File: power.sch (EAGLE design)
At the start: 7 parts, among them U1 LT3652

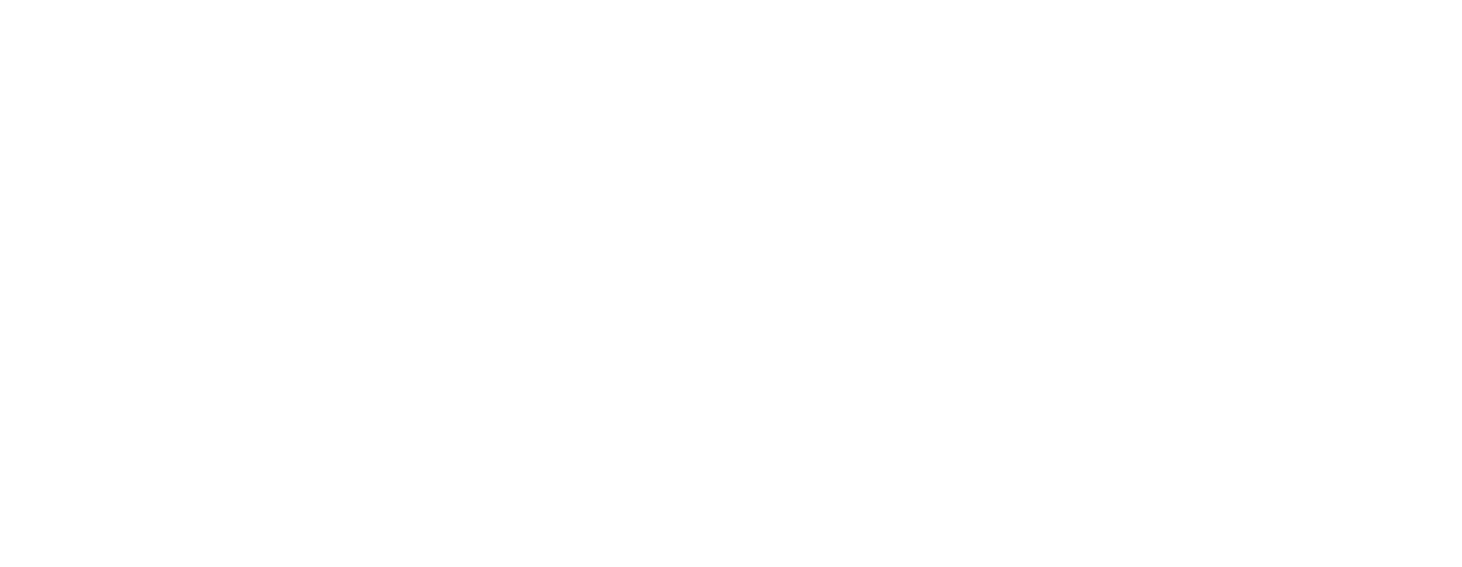
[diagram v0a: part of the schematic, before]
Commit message: Added RTC backup batteries
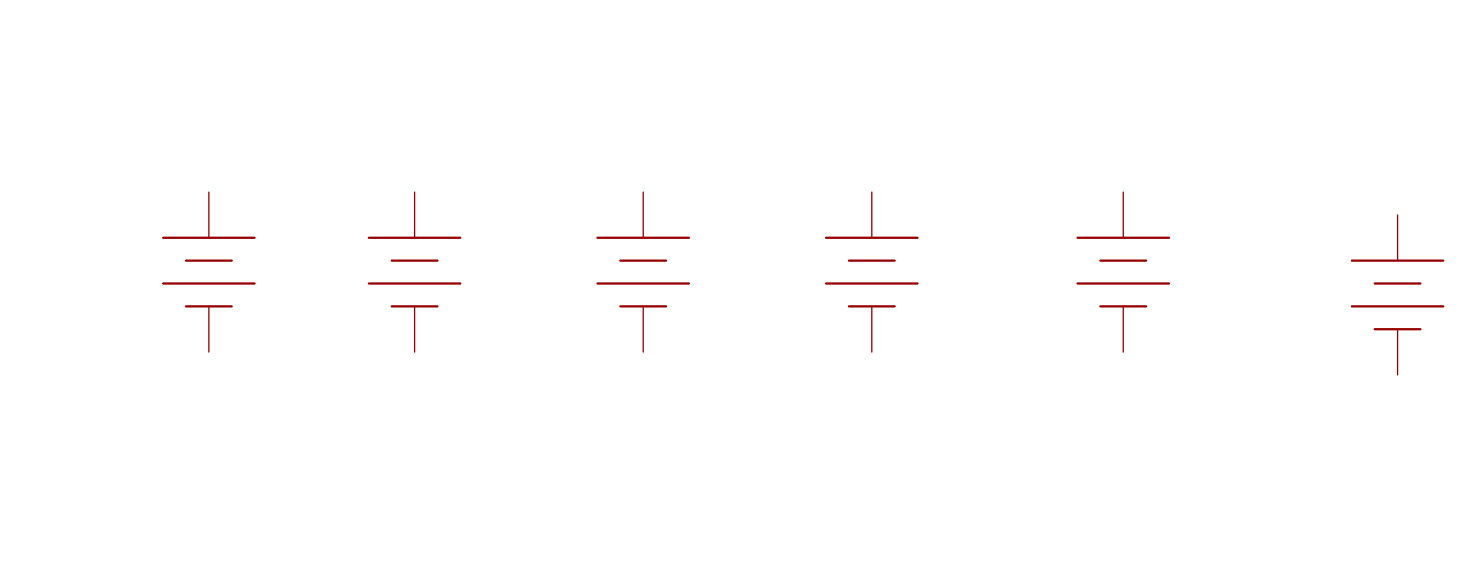
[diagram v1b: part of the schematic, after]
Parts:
- added U$10, U$11, U$12, U$7, U$8, U$9: BETABATTERY, Widetronix:BETABATTERY
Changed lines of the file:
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@@
 <part name="U$5" library="G125-FV20605L0P" deviceset="G125-FV20605L0P" device=""/>
 <part name="U$6" library="G125-FV20605L0P" deviceset="G125-FV20605L0P" device=""/>
+<part name="U$7" library="Widetronix" deviceset="BETABATTERY" device=""/>
+<part name="U$8" library="Widetronix" deviceset="BETABATTERY" device=""/>
+<part name="U$9" library="Widetronix" deviceset="BETABATTERY" device=""/>
+<part name="U$10" library="Widetronix" deviceset="BETABATTERY" device=""/>
+<part name="U$11" library="Widetronix" deviceset="BETABATTERY" device=""/>
+<part name="U$12" library="Widetronix" deviceset="BETABATTERY" device=""/>
 </parts>
 <sheets>
@@
 <instance part="U$5" gate="G$1" x="73.66" y="81.28" rot="R90"/>
 <instance part="U$6" gate="G$1" x="114.3" y="86.36" rot="R90"/>
+<instance part="U$7" gate="G$1" x="167.64" y="66.04"/>
+<instance part="U$8" gate="G$1" x="190.5" y="66.04"/>
+<instance part="U$9" gate="G$1" x="215.9" y="66.04"/>
+<instance part="U$10" gate="G$1" x="241.3" y="66.04"/>
+<instance part="U$11" gate="G$1" x="269.24" y="66.04"/>
+<instance part="U$12" gate="G$1" x="299.72" y="63.5"/>
 </instances>
 <busses>

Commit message: Power board work
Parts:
- added H1, H2: PINHD-2X26, SparkFun-Connectors:PINHD-2X26
- added J1: POWER_JACKPTH_BREAD, SparkFun-Connectors:POWER_JACKPTH_BREAD
- added JP1, JP2, JP3: M025MM, SparkFun-Connectors:M025MM
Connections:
- new net 3.3V: H2.27, H2.28
- new net 5V: H2.25, H2.26
- new net GND: H2.29, H2.30, H2.31, H2.32, J1.GND, J1.GNDBREAK, JP1.1, JP2.1, JP3.1, U$10.V-, U$11.V-, U$12.V-, U$7.V-, U$8.V-, U$9.V-, U1.GND_PAD
- new net SCL: H1.43
- new net SDA: H1.41
- new net VBACKUP: H1.42, U$10.V+, U$11.V+, U$12.V+, U$7.V+, U$8.V+, U$9.V+
- new net VBATT: H2.45, H2.46, J1.PWR, JP1.2, JP2.2
- new net VBURN3: JP3.2

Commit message: Added LT3688 dual regulator
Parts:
- added C1, C2, C30: .1uF, phonesat:CAPACITOR0805
- added R1, R25, R31, R4, R5, R8: 0R, phonesat:RESISTOR2512
- added R2, R27, R6: 3K3, phonesat:RESISTOR0805
- added R28, R3, R7: 10K, phonesat:RESISTOR0805
- added T1, T2, T3: SINGLE_NCHAN_FET, phonesat:SINGLE_NCHAN_FET
- added U$13: LT3688, LT3688:LT3688
- added U14, U2: MOSFET_PCHAN_20A, phonesat:MOSFET_PCHAN_20A
- U1: value LT3652 -> MOSFET_PCHAN_20A; device SparkFun-PowerIC:LT3652 -> phonesat:MOSFET_PCHAN_20A
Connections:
- new net ENAB_BURN1: R28.1, R3.1, R7.1
- new net N$1: R1.2, R4.2, U1.S@1, U1.S@2, U1.S@3
- new net N$19: R25.2, R31.2, U14.S@1, U14.S@2, U14.S@3
- new net N$2: C1.1, R3.2, T1.G
- new net N$21: C30.1, R28.2, T2.G
- new net N$24: R27.1, T2.D, U14.G
- new net N$3: R2.1, T1.D, U1.G
- new net N$4: R5.2, R8.2, U2.S@1, U2.S@2, U2.S@3
- new net N$5: C2.1, R7.2, T3.G
- new net N$6: R6.1, T3.D, U2.G
- new net VBURN1: U14.D@1, U14.D@2, U14.D@3, U14.D@4
- new net VBURN2: U1.D@1, U1.D@2, U1.D@3, U1.D@4
- new net VCC_8: R1.1, R2.2, R25.1, R27.2, R31.1, R4.1, R5.1, R6.2, R8.1
- new net VSOLAR: U$5.P3, U$5.P6
- net GND: now also C1.2, C2.2, C30.2, T1.S, T2.S, T3.S, U$1.P1, U$1.P4, U$2.P1, U$2.P4, U$3.P1, U$3.P4, U$4.P1, U$4.P4, U$5.P1, U$5.P4, U$6.P1, U$6.P4; no longer U1.GND_PAD
- net VBURN3: now also U2.D@1, U2.D@2, U2.D@3, U2.D@4
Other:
- note added: "BW1"
- note added: "BW2"
- note added: "BW3"

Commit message: More switching regulator work
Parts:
- added C3, C4, C5: 0.22uF, SparkFun-Capacitors:CAP0805
- added C31, C32: .1uF, phonesat:CAPACITOR0805
- added C6, C7: 10pF, SparkFun-Capacitors:CAP0805
- added C8, C9: 1nF, SparkFun-Capacitors:CAP0805
- added R11: 523k, SparkFun-Resistors:RESISTOR0805-RES
- added R12, R14: 100k, SparkFun-Resistors:RESISTOR0805-RES
- added R13: 316k, SparkFun-Resistors:RESISTOR0805-RES
- added R9: 10k, SparkFun-Resistors:RESISTOR0805-RES
- C1: value .1uF -> 4.7uF; device phonesat:CAPACITOR0805 -> SparkFun-Capacitors:CAP0805
- C2: value .1uF -> 0.22uF; device phonesat:CAPACITOR0805 -> SparkFun-Capacitors:CAP0805
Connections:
- new net N$11: C3.1, U$13.BST2
- new net N$12: C6.2, R11.1, R12.2, U$13.FB1
- new net N$13: C8.2, U$13.RUNSS1
- new net N$14: C7.2, R13.1, R14.2, U$13.FB2
- new net N$7: R9.1, U$13.EN
- new net N$8: C9.1, U$13.RUNSS2
- new net N$9: C2.1, U$13.BST1
- net 3.3V: now also C3.2, C5.1, C7.1, R13.2, U$13.BIAS, U$13.SW2
- net 5V: now also C2.2, C4.1, C6.1, R11.2, U$13.SW1
- net GND: now also C31.2, C32.2, C4.2, C5.2, C8.1, C9.2, R12.1, R14.1, U$13.GND, U$13.~WDE; no longer C2.2
- net N$2: now also C31.1; no longer C1.1
- net N$5: now also C32.1; no longer C2.1
- net VBATT: now also C1.1, R9.2, U$13.VIN
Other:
- moved on the sheet: C1, C2

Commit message: Finished regulator circuit design
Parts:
- removed R1, R25, R31, R4, R5, R8: 0R, phonesat:RESISTOR2512
- added C10, C11: 4.7uF, SparkFun-Capacitors:CAP0805
- added D1, D2: BAT20J, SparkFun-DiscreteSemi:DIODE-SCHOTTKY-BAT20J
- added L1, L2: SLF10145, SLF10145:SLF10145
- added R10: 110k, SparkFun-Resistors:RESISTOR0805-RES
- C4, C5: value 0.22uF -> 22uF; device SparkFun-Capacitors:CAP0805 -> SparkFun-Capacitors:CAP1210
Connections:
- removed net N$1: R1.2, R4.2, U1.S@1, U1.S@2, U1.S@3
- removed net N$19: R25.2, R31.2, U14.S@1, U14.S@2, U14.S@3
- removed net N$4: R5.2, R8.2, U2.S@1, U2.S@2, U2.S@3
- removed net VCC_8: R1.1, R2.2, R25.1, R27.2, R31.1, R4.1, R5.1, R6.2, R8.1
- new net N$10: C2.2, D1.C, L1.P2, U$13.SW1
- new net N$15: C3.2, D2.C, L2.P1, U$13.SW2
- new net N$16: D1.A, U$13.DA1
- new net N$17: D2.A, U$13.DA2
- new net N$18: R10.2, U$13.RT
- new net N$20: C10.1, U$13.CPOR2
- new net N$22: C11.1, U$13.CPOR1
- net 3.3V: now also L2.P2; no longer C3.2, U$13.SW2
- net 5V: now also L1.P1, U$13.~WDE; no longer C2.2, U$13.SW1
- net GND: now also C10.2, C11.2, R10.1, U$13.SYNC; no longer U$13.~WDE
- net VBATT: now also R2.2, R27.2, R6.2, U1.S@1, U1.S@2, U1.S@3, U14.S@1, U14.S@2, U14.S@3, U2.S@1, U2.S@2, U2.S@3
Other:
- note added: "15uH"
- note added: "22uH"
- note added: "L1"
- note added: "L2"
- moved on the sheet: C4, C5, C6, C7, R11, R12, R13, R14

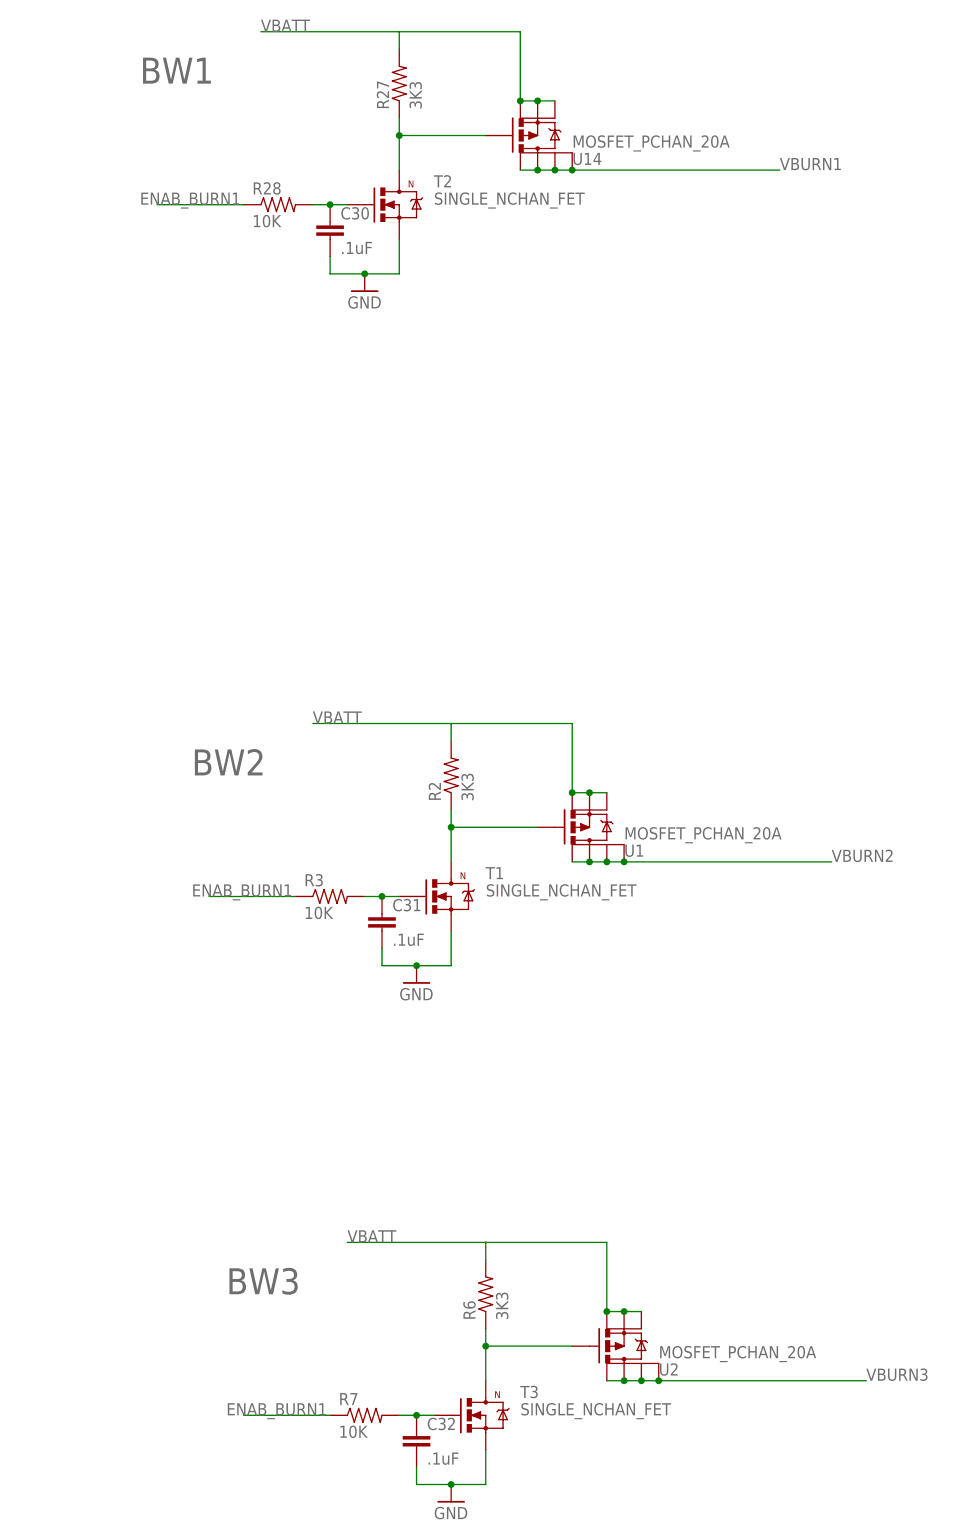
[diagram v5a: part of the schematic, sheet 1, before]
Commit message: Added foot switch terminals to power board
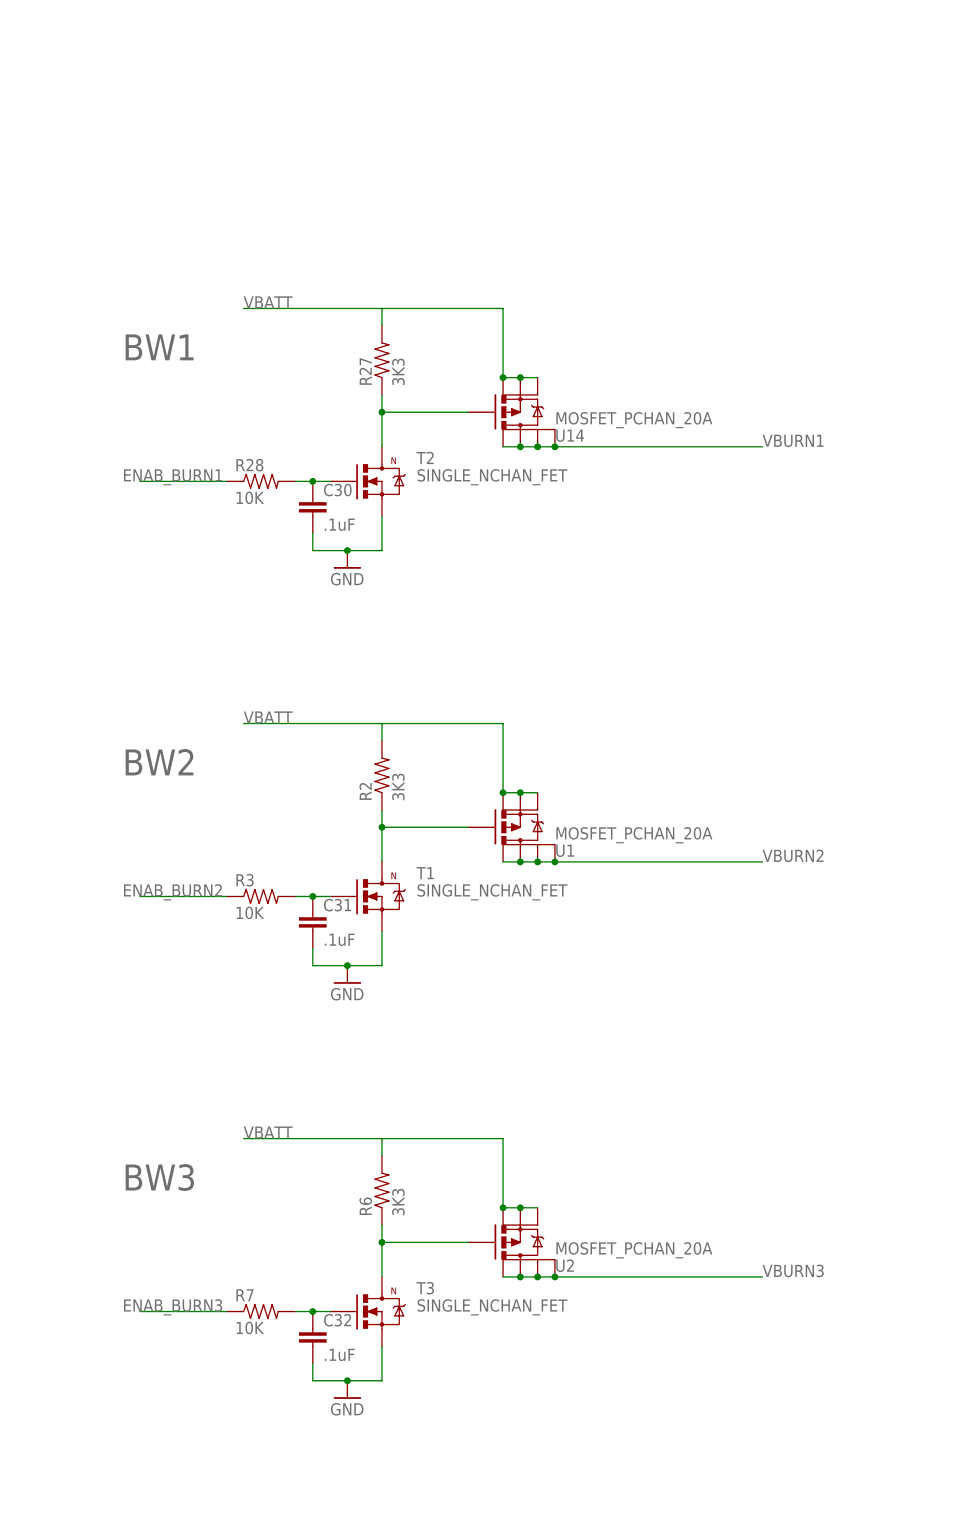
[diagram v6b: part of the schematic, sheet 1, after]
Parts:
- added JP4, JP5: M025MM, SparkFun-Connectors:M025MM
- added R1, R4: 0R, rcl:R-US_R1210
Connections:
- new net BATT_INPUT: J1.PWR, JP1.2, JP2.2, JP4.2, R1.1
- new net ENAB_BURN2: R3.1
- new net ENAB_BURN3: R7.1
- new net N$4: JP4.1, JP5.2, R1.2, R4.1
- net ENAB_BURN1: no longer R3.1, R7.1
- net VBATT: now also JP5.1, R4.2; no longer J1.PWR, JP1.2, JP2.2
- net VBURN1: now also U$6.P2, U$6.P5
- net VBURN2: now also U$1.P2, U$1.P5
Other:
- note added: "Battery Terminals"
- note added: "Burn Wire 3 Terminal"
- note added: "CubeSat Bus Connectors"
- note added: "External Battery Charger Jack"
- note added: "Footswitch Connections"
- note added: "Optional for 0, 1, or 2 footswitches"
- note added: "Solar Panel Connectors"
- moved on the sheet: C30, C31, C32, J1, JP1, JP2, JP3, R2, R27, R28, R3, R6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
